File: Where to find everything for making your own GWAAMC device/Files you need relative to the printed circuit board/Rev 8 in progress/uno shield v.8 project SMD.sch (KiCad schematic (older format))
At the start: 108 parts, among them J1 Conn_3.5mm, J2 Power, J3 Analog, J4 Digital, J5 Digital, J6 Conn_01x09_Female, J6_A7,A6 Conn_01x02_gender_unknown, J7_A7,A6 Conn_01x02_Female, J9 TE_1-2328702-0, P1 CONN_01X01, P2 CONN_01X01, P3 CONN_01X01, P4 CONN_01X01, Q1 MMBF5460 (2N5460), Q2 MMBF5460 (2N5460), Q3 DMN601K-7, Q4 DMN601K-7, Q5 DMN601K-7, Q6 DMN601K-7, Q7 DMN601K-7, U1 3V LDO, U10 MCP4262-502E/UN, U11 MCP4262-502E/UN, U12 MCP4262-502E/UN, U13 MCP4262-502E/UN, U14 MCP4262-502E/UN, U15 MCP4262-502E/UN, U16 MCP4262-502E/UN, U17 MCP4262-502E/UN, U18 MCP4262-502E/UN, U19 MCP4262-502E/UN, U2 AD8244ARMZ, U20 MCP4262-502E/UN, U21 MCP4262-502E/UN, U22 MCP4262-502E/UN, U23 MCP4262-502E/UN, U24 MCP4262-502E/UN, U25 MCP4262-502E/UN, U26 MCP4262-502E/UN, U27 MCP4262-502E/UN, U28 MCP4262-502E/UN, U29 MCP4262-502E/UN, U3 ADL5315ACPZ-R7, U30 MCP4262-502E/UN, U31 MCP4262-502E/UN, U32 MCP4262-502E/UN, U33 MCP4262-502E/UN, U4 REF200AU, U5 LM334M, U6 LM334M, U7 MCP4262-503E/UN, U8 - U32 all in parallel MCP4262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, U9 MCP4262-502E/UN

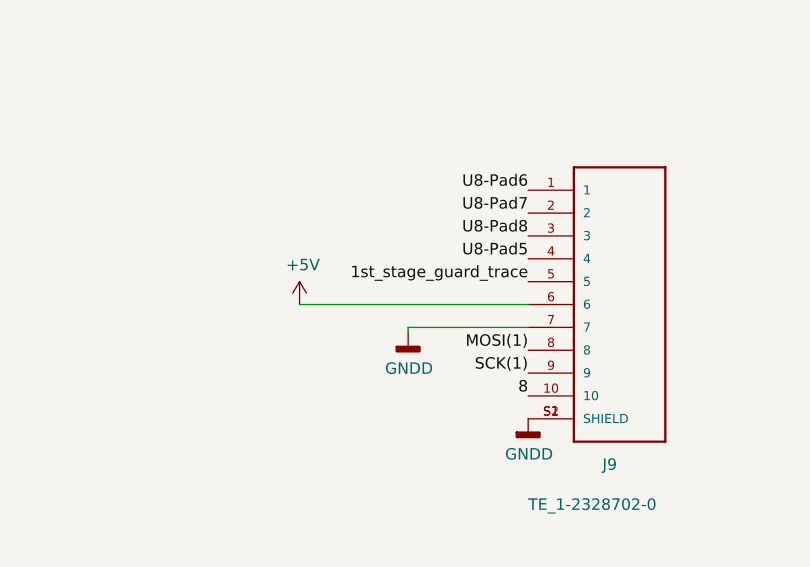
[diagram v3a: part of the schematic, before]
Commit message: Untested while awaiting bare PCB boards....
These KiCad and zipped gerber files are fully designed but not yet tested while I await the bare boards on order now.  I'm estimating mid- to late-October will see the final evaluation of operation of the entire device.  Shortly after that, I would expect to demonstrate its concepts and operation via YouTube and personal travel.
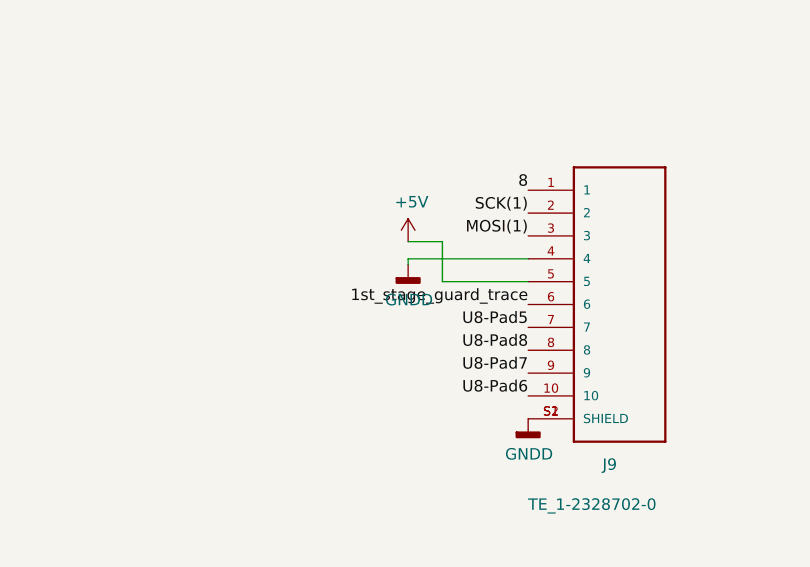
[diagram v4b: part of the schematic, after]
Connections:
- net +5V: now also J9.5; no longer J9.6
- net 1st_stage_guard_trace: now also J9.6; no longer J9.5
- net 8: now also J9.1; no longer J9.10
- net GNDD: now also J9.4; no longer J9.7
- net MOSI(1): now also J9.3; no longer J9.8
- net SCK(1): now also J9.2; no longer J9.9
- net U8-Pad5: now also J9.7; no longer J9.4
- net U8-Pad6: now also J9.10; no longer J9.1
- net U8-Pad7: now also J9.9; no longer J9.2
- net U8-Pad8: now also J9.8; no longer J9.3
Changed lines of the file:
@@
 L power:+5V #PWR0143
 U 1 1 5D764CDA
-P 3950 -800
-F 0 "#PWR0143" H 3950 -950 50  0001 C CNN
-F 1 "+5V" H 3965 -627 50  0000 C CNN
-F 2 "" H 3950 -800 50  0001 C CNN
-F 3 "" H 3950 -800 50  0001 C CNN
-	1    3950 -800
+P 4425 -1075
+F 0 "#PWR0143" H 4425 -1225 50  0001 C CNN
+F 1 "+5V" H 4440 -902 50  0000 C CNN
+F 2 "" H 4425 -1075 50  0001 C CNN
+F 3 "" H 4425 -1075 50  0001 C CNN
+	1    4425 -1075
 	1    0    0    -1
 $EndComp
-Text Label 4950 -400 2    50   ~ 0
+Text Label 4950 -1300 2    50   ~ 0
 8
-Text Label 4950 -500 2    50   ~ 0
+Text Label 4950 -1200 2    50   ~ 0
 SCK(1)
-Text Label 4950 -600 2    50   ~ 0
+Text Label 4950 -1100 2    50   ~ 0
 MOSI(1)
-Wire Wire Line
-	4950 -800 3950 -800
 $Comp
 L power:GNDD #PWR0144
 U 1 1 5D79F70A
-P 4425 -675
-F 0 "#PWR0144" H 4425 -925 50  0001 C CNN
-F 1 "GNDD" H 4429 -830 50  0000 C CNN
-F 2 "" H 4425 -675 50  0001 C CNN
-F 3 "" H 4425 -675 50  0001 C CNN
-	1    4425 -675
+P 4425 -975
+F 0 "#PWR0144" H 4425 -1225 50  0001 C CNN
+F 1 "GNDD" H 4429 -1130 50  0000 C CNN
+F 2 "" H 4425 -975 50  0001 C CNN
+F 3 "" H 4425 -975 50  0001 C CNN
+	1    4425 -975
 	1    0    0    -1
 $EndComp
-Text Label 4950 -1000 2    50   ~ 0
+Text Label 4950 -700 2    50   ~ 0
 U8-Pad5
-Text Label 4950 -1300 2    50   ~ 0
+Text Label 4950 -400 2    50   ~ 0
 U8-Pad6
-Text Label 4950 -1200 2    50   ~ 0
+Text Label 4950 -500 2    50   ~ 0
 U8-Pad7
-Text Label 4950 -1100 2    50   ~ 0
+Text Label 4950 -600 2    50   ~ 0
 U8-Pad8
 Wire Wire Line
-	4950 -700 4425 -700
+	4950 -1000 4425 -1000
 Wire Wire Line
-	4425 -700 4425 -675
-Text Label 4950 -900 2    50   ~ 0
+	4425 -1000 4425 -975
+Text Label 4950 -800 2    50   ~ 0
 1st_stage_guard_trace
 $Comp
@@
 Text Label 11450 4425 0    50   ~ 0
 8
+Wire Wire Line
+	4950 -900 4575 -900
+Wire Wire Line
+	4575 -900 4575 -1075
+Wire Wire Line
+	4575 -1075 4425 -1075
 $EndSCHEMATC

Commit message: Untested while awaiting bare PCB boards....
These KiCad and zipped gerber files are fully designed but not yet tested while I await the bare boards on order now.  I'm estimating mid- to late-October will see the final evaluation of operation of the entire device.  Shortly after that, I would expect to demonstrate its concepts and operation via YouTube and personal travel.
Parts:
- ADC1: Source Sockets: 1 qty SL-106-T-10 + 1 qty SMC-1-04-1-GT from http://Arrow.com. Component: least cost - https://www.aliexpress.com/item/1PCS-X-HX711-modules-weigh-sensors-for-AD-module-chip-preferred-DIY-Graduation/32851591970.html?spm=2114.search0104.3.1.7ad07d02cMfLjw&ws_ab_test=searchweb0_0,searchweb201602_4_10065_10130_10068_10890_10547_319_10546_317_10548_10545_10696_453_10084_454_10083_10618_10307_537_536_10059_10884_10887_321_322_10103,searchweb201603_52,ppcSwitch_0&algo_expid=c46a3ce9-e8cf-4d7c-8e89-50e4aff4f628-0&algo_pvid=c46a3ce9-e8cf-4d7c-8e89-50e4aff4f628&transAbTest=ae803_3; fastest arrival https://www.ebay.com/itm/Dual-Channel-HX711-Weighing-Pressure-Sensor-24-bit-Precision-A-D-Module-Arduino/202679288819?hash=item2f30a083f3:g:xyIAAOSwhXtc2wdH -> Sockets: 1 qty SL-106-T-10 + 1 qty SMC-1-04-1-GT from http://Arrow.com (sockets only, remember). Component: least cost - https://www.aliexpress.com/item/1PCS-X-HX711-modules-weigh-sensors-for-AD-module-chip-preferred-DIY-Graduation/32851591970.html?spm=2114.search0104.3.1.7ad07d02cMfLjw&ws_ab_test=searchweb0_0,searchweb201602_4_10065_10130_10068_10890_10547_319_10546_317_10548_10545_10696_453_10084_454_10083_10618_10307_537_536_10059_10884_10887_321_322_10103,searchweb201603_52,ppcSwitch_0&algo_expid=c46a3ce9-e8cf-4d7c-8e89-50e4aff4f628-0&algo_pvid=c46a3ce9-e8cf-4d7c-8e89-50e4aff4f628&transAbTest=ae803_3; fastest arrival https://www.ebay.com/itm/Dual-Channel-HX711-Weighing-Pressure-Sensor-24-bit-Precision-A-D-Module-Arduino/202679288819?hash=item2f30a083f3:g:xyIAAOSwhXtc2wdH
- C1: ClickToSortForPlacement 02 A duplicate C1 pad set is on PCB. Determine which pad se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 -> 02 A tiny 0201-size duplicate C1 pad set is on PCB. Determi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
- FID1, FID2, FID3, FID4, FID5, FID6: Source (none) -> 0 For clarity: [If not shown] U9-U33 must be ordered as wel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
- JP1: ClickToSortForPlacement 00 (TIPS - Always when sorting this page, make the column's title cell show the little sort direction indicator highlighted and pointing up. Solder temperature if using a soldering iron: Highest temperature solder when used for two-lead SMD components so they aren't so easily dislocated when bumped with hot iron. Never allow leaded solder to cross contaminate low-temp [bismuth] solders - lead ruins them. Plated through holes can only be used once on new boards unless they are HASL and you are careful to match solders with the factory solder or you are prepared to ream out plating-contaminated solder from the hole, so do NOT assume that tinning plated through holes to prepare the holes themselves for pins or leads is the right thing to do! Just use them as-is when the time comes even though they won't take the solder as well, or instead you may plug the holes with stainless steel paste dispensing syringe needle/nozzle 20-21 gauge while you tin the annular ring only on the one side oppo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 -> 00 (TIPS - Always when sorting this page, make the column's title cell show the little sort direction indicator highlighted and pointing up. Solder temperature if using a soldering iron: Highest temperature solder when used for two-lead SMD components so they aren't so easily dislocated when bumped with hot iron. Never allow leaded solder to cross contaminate low-temp [bismuth] solders - lead ruins them. Plated through holes can only be used once on new boards unless they are HASL and you are careful to match solders with the factory solder or you are prepared to ream out plating-contaminated solder from the hole, so do NOT assume that tinning plated through holes to prepare the holes themselves for pins or leads is the right thing to do! Just use them as-is when the time comes even though they won't take the solder as well, or instead you may plug the holes with stainless steel paste dispensing syringe needle/nozzle 20-21 gauge while you tin the annular ring only on the one side oppo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
- P1, P2, P3, P4: Source n/a -> 0 For clarity: [If not shown] U9-U33 must be ordered as wel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
- U10, U11, U12, U13, U14, U15, U16, U17, U18, U19, U20, U21, U22, U23, U24, U25, U26, U27, U28, U29, U30, U31, U32, U33, U9: Source http://www.digikey.com -> http://digikey.com
- U7: Source http://www.Arrow.com -> http://Arrow.com
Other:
- note added: "1 step MSB is 50000 ohms per device/256 steps per device = 195.3125 ohms = 195 ohms\n\n 5000 ohms LSB:\na single LSB device full resistance is 5000 ohms per device\n\nnumber of LSB devices to parallel together to make their full resistance value equal to 195 ohms is 5000 ohms per device/195 ohms = 25.6 devices\n\ncost = $25 + flex board a little larger size\n\n Alternate design under consideratio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"
- note added: "· 1 roll Polyimide (Kapton) tape 3/8" wide 6' length or greater. Use as electrical insulator and place assist. P/N 3057 from Arrow \nor equivalent\n· 38ga magnet wire for trace repairs. P/N 3522 from Arrow or equivalent\n· Solder wick P/N TOL-09327 from Arrow or equivalent\n· Soldering colophony (pine or gum ROSIN - NOT with zinc or ammonium chloride) flux (can make it yourself)\n· RG316 Coaxial 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"
- note removed: "1 roll Polyimide tape 3/8" wide 6' length or greater. Use as electrical insulator and place assist. P/N 3057 from Arrow or equivalent\n\n38ga magnet wire for U8+ and for trace repairs. P/N 3522 from Arrow or equivalent\nVery high temp solder (K100) not allowed on U3.\nThe best solder will always be "No Heat SAC305" if you can find it, but you still MUST cleanse gold from pads.\nAvoid Pb (leaded) 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"
- moved on the sheet: J9

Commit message: Untested while I'm building it out
These KiCad and zipped gerber files are fully designed but not yet tested while I'm building the bare boards now.  I'm estimating mid- to late-October will see the final evaluation of operation of the entire device.
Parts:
- ICSP1: ClickToSortForPlacement 19 Remove the previous JP6 wire and hold the full-size JP6 in its place while placing this. Set height with all connectors to MCU mated, some connectors may need spaced away from board or otherwise made to fit. Then check work for inadvertent shorts and opens. Replace JP6, if removed, with the style you want - wire or removeable shunt. Apply Kapton tape anywhere needed as board is mated to MCU, while also ensuring no Vcc conflicts will exist. -> 19 Remove the previous JP6 wire and hold the full-size JP6 in its place while placing this. Set height with all connectors to MCU mated, some connectors may need spaced away from board or otherwise made to fit. Place using bismuth solder if you have it (provided you used no-lead solder to pre-tin with) for easiest removal. Then check work for inadvertent shorts and opens. Replace JP6, if removed, with the style you want - wire or removeable shunt. Apply Kapton tape anywhere needed as board is mated to MCU, while also ensuring no Vcc conflicts will exist.
- J2: ClickToSortForPlacement 20 When MCU is NOT 5V, pin 5 gets removed and pin 4 gets its pad shorted to pin 5 PAD. When MCU is switchable 5V and 3.3V and you want to be able to switch between the two levels, remove pin 5 still but tie ICSP1 pin 2 into pin 5 PAD with an insulated wire. Height with all connectors mated, may need to space away from board some. Then check work for inadvertent shorts and opens. -> 20 When MCU is NOT 5V, pin 5 gets removed and pin 4 gets its pad shorted to pin 5 PAD. When MCU is switchable 5V and 3.3V and you want to be able to switch between the two levels, remove pin 5 still but tie ICSP1 pin 2 into pin 5 PAD with an insulated wire. Height with all connectors mated, may need to space away from board some. Place with dessicant inside using bismuth solder if you have it for easiest removal (provided you used no-lead solder to pre-tin with) . Then check work for inadvertent shorts and opens.
- J3, J4: ClickToSortForPlacement 20 Placing into plated-through holes requires more solder t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 -> 20 Requires more solder than single-sided components and he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
- J5: ClickToSortForPlacement 21 Set height with all connectors mated, may need to space away from board some. Placing into plated-through holes requires more solder than single-sided components and heat for a longer time or the MCU can push the solder pads right off the board. Then check work for inadvertent shorts and opens. Power up and run diags. Power down and continue. -> 21 Set height with all connectors mated, may need to space away from board some. Requires more solder than single-sided components and heat for a longer time or the MCU can push the solder pads right off the board. Use bismuth solder if you have it for easiest removal (provided you used no-lead solder to pre-tin with). Then check work for inadvertent shorts and opens. Power up and run diags. Power down and continue.
- JP1: footprint Jumper:SolderJumper-3_P1.3mm_Open_RoundedPad1.0x1.5mm_NumberLabels -> Jumper:SolderJumper-3_P1.3mm_Bridged12_RoundedPad1.0x1.5mm_NumberLabels; symbol Jumper:SolderJumper_3_Open -> Jumper:SolderJumper_3_Bridged12; ClickToSortForPlacement 00 (TIPS - Always when sorting this page, make the column's title cell show the little sort direction indicator highlighted and pointing up. Solder temperature if using a soldering iron: Highest temperature solder when used for two-lead SMD components so they aren't so easily dislocated when bumped with hot iron. Never allow leaded solder to cross contaminate low-temp [bismuth] solders - lead ruins them. Plated through holes can only be used once on new boards unless they are HASL and you are careful to match solders with the factory solder or you are prepared to ream out plating-contaminated solder from the hole, so do NOT assume that tinning plated through holes to prepare the holes themselves for pins or leads is the right thing to do! Just use them as-is when the time comes even though they won't take the solder as well, or instead you may plug the holes with stainless steel paste dispensing syringe needle/nozzle 20-21 gauge while you tin the annular ring only on the one side oppo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 -> 00 (TIPS - Always when sorting this page, make the column's title cell show the little sort direction indicator highlighted and pointing up. Solder temperature if using a soldering iron: Use your highest temperature solder for two-lead SMD components so they aren't so easily dislocated later when accidentally bumped with hot iron. Never allow leaded solder to cross contaminate low-temp [bismuth] solders - lead ruins them. Do your best to keep SMD component leads clean from adhesive tape glue and other sticky, clingy, slimy contaminates that could leave a film where solder will need to adhere to them. Plated through holes can only be used once on new boards unless they are Hot Air Solder Leveled [HASL] and you are careful to match solders with the factory solder or you are prepared to ream out plating-contaminated solder from the hole, so do NOT assume that tinning plated through holes to prepare the holes themselves for pins or leads is the right thing to do! Just use them as-is when 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
- JP2: footprint Jumper:SolderJumper-3_P1.3mm_Open_RoundedPad1.0x1.5mm_NumberLabels -> Jumper:SolderJumper-3_P1.3mm_Bridged12_RoundedPad1.0x1.5mm_NumberLabels; symbol Jumper:SolderJumper_3_Open -> Jumper:SolderJumper_3_Bridged12
- R17: ClickToSortForPlacement 14 IF NO FOOTPRINT FOR THIS: OPTIONAL IN BOARD REV 7 AND BE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 -> 14 IF NO FOOTPRINT FOR THIS: OPTIONAL IN BOARD REV .7 AND B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
- R5: ClickToSortForPlacement 05 Place, then check work as before. The steps up to this one were to install amplification stability ckt for powering up U2. Pwr supply stability ckts for U1 and ADC1 are next after diagnostics of the work you've done so far: You have reached the step of applying power voltage to the board, and you MUST not make any mistakes doing so or you'll all too likely damage components that will cost you extra shipping, handling to replace. As you prepare to continue, be fully aware that any mistakes you make can destroy components when power gets applied. BE VERY OBSERVANT. Determine which of +5V or +3V3 your MCU puts on ICSP1 pin 2 before applying MCU power to this board: 5V is default of this PCB design. If the MCU instead puts 3V on the ICSP1 pin 2, you MUST modify this board at J2 pins 4 & 5 or you'll stress out your MCU and likely damage it! Such modification inflexibly renders this board unfit for 5V operation since there was not room for jumpers to make this change flexible. You will b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 -> 05 Place, then check work as before. The steps up to this one were to install first stage stability ckt for powering up U3. Pwr supply stability ckts for U1 and ADC1 are next after diagnostics of the work you've done so far: You have reached the step of applying power voltage to the board, and you MUST not make any mistakes doing so or you'll all too likely damage components that will cost you extra shipping, handling to replace. As you prepare to continue, be fully aware that any mistakes you make can destroy components when power gets applied. BE VERY OBSERVANT. Determine which of +5V or +3V3 your MCU puts on ICSP1 pin 2 before applying MCU power to this board: 5V is default of this PCB design. If the MCU instead puts 3V on the ICSP1 pin 2, you MUST modify this board at J2 pins 4 & 5 or you'll stress out your MCU and likely damage it! Such modification inflexibly renders this board unfit for 5V operation since there was not room for jumpers to make this change flexible. You will bri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
- SHLD1: ClickToSortForPlacement 27 Thoroughly solder in place with dessicant inside. Verify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 -> 27 Verify every place-assist hole inside shield footprint i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
- U10: renamed from U13; ClickToSortForPlacement 15 NOT WELL ACCOMMODATED ON BOARD REV 7 AND BELOW: PATCHING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 -> 15 NOT WELL ACCOMMODATED ON BOARD REV .7 AND BELOW: PATCHIN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
- U11: renamed from U17; ClickToSortForPlacement 15 NOT WELL ACCOMMODATED ON BOARD REV 7 AND BELOW: PATCHING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 -> 15 NOT WELL ACCOMMODATED ON BOARD REV .7 AND BELOW: PATCHIN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
- U12: renamed from U21; ClickToSortForPlacement 15 NOT WELL ACCOMMODATED ON BOARD REV 7 AND BELOW: PATCHING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 -> 15 NOT WELL ACCOMMODATED ON BOARD REV .7 AND BELOW: PATCHIN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
- U13: renamed from U25; ClickToSortForPlacement 15 NOT WELL ACCOMMODATED ON BOARD REV 7 AND BELOW: PATCHING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 -> 15 NOT WELL ACCOMMODATED ON BOARD REV .7 AND BELOW: PATCHIN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
- U14: renamed from U29; ClickToSortForPlacement 15 NOT WELL ACCOMMODATED ON BOARD REV 7 AND BELOW: PATCHING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 -> 15 NOT WELL ACCOMMODATED ON BOARD REV .7 AND BELOW: PATCHIN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
- U15: renamed from U10; ClickToSortForPlacement 15 NOT WELL ACCOMMODATED ON BOARD REV 7 AND BELOW: PATCHING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 -> 15 NOT WELL ACCOMMODATED ON BOARD REV .7 AND BELOW: PATCHIN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
- U16: renamed from U14; ClickToSortForPlacement 15 NOT WELL ACCOMMODATED ON BOARD REV 7 AND BELOW: PATCHING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 -> 15 NOT WELL ACCOMMODATED ON BOARD REV .7 AND BELOW: PATCHIN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
- U17: renamed from U18; ClickToSortForPlacement 15 NOT WELL ACCOMMODATED ON BOARD REV 7 AND BELOW: PATCHING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 -> 15 NOT WELL ACCOMMODATED ON BOARD REV .7 AND BELOW: PATCHIN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
- U18: renamed from U22; ClickToSortForPlacement 15 NOT WELL ACCOMMODATED ON BOARD REV 7 AND BELOW: PATCHING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 -> 15 NOT WELL ACCOMMODATED ON BOARD REV .7 AND BELOW: PATCHIN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
- U19: renamed from U26; ClickToSortForPlacement 15 NOT WELL ACCOMMODATED ON BOARD REV 7 AND BELOW: PATCHING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 -> 15 NOT WELL ACCOMMODATED ON BOARD REV .7 AND BELOW: PATCHIN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
- U20: renamed from U30; ClickToSortForPlacement 15 NOT WELL ACCOMMODATED ON BOARD REV 7 AND BELOW: PATCHING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 -> 15 NOT WELL ACCOMMODATED ON BOARD REV .7 AND BELOW: PATCHIN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
- U21: renamed from U11; ClickToSortForPlacement 15 NOT WELL ACCOMMODATED ON BOARD REV 7 AND BELOW: PATCHING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 -> 15 NOT WELL ACCOMMODATED ON BOARD REV .7 AND BELOW: PATCHIN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
- U22: renamed from U15; ClickToSortForPlacement 15 NOT WELL ACCOMMODATED ON BOARD REV 7 AND BELOW: PATCHING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 -> 15 NOT WELL ACCOMMODATED ON BOARD REV .7 AND BELOW: PATCHIN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
- U23: renamed from U19; ClickToSortForPlacement 15 NOT WELL ACCOMMODATED ON BOARD REV 7 AND BELOW: PATCHING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 -> 15 NOT WELL ACCOMMODATED ON BOARD REV .7 AND BELOW: PATCHIN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
- U24: renamed from U23; ClickToSortForPlacement 15 NOT WELL ACCOMMODATED ON BOARD REV 7 AND BELOW: PATCHING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 -> 15 NOT WELL ACCOMMODATED ON BOARD REV .7 AND BELOW: PATCHIN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
- U25: renamed from U27; ClickToSortForPlacement 15 NOT WELL ACCOMMODATED ON BOARD REV 7 AND BELOW: PATCHING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 -> 15 NOT WELL ACCOMMODATED ON BOARD REV .7 AND BELOW: PATCHIN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
- U26: renamed from U31; ClickToSortForPlacement 15 NOT WELL ACCOMMODATED ON BOARD REV 7 AND BELOW: PATCHING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 -> 15 NOT WELL ACCOMMODATED ON BOARD REV .7 AND BELOW: PATCHIN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
- U27: renamed from U12; ClickToSortForPlacement 15 NOT WELL ACCOMMODATED ON BOARD REV 7 AND BELOW: PATCHING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 -> 15 NOT WELL ACCOMMODATED ON BOARD REV .7 AND BELOW: PATCHIN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
- U28: renamed from U16; ClickToSortForPlacement 15 NOT WELL ACCOMMODATED ON BOARD REV 7 AND BELOW: PATCHING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 -> 15 NOT WELL ACCOMMODATED ON BOARD REV .7 AND BELOW: PATCHIN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
- U29: renamed from U20; ClickToSortForPlacement 15 NOT WELL ACCOMMODATED ON BOARD REV 7 AND BELOW: PATCHING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 -> 15 NOT WELL ACCOMMODATED ON BOARD REV .7 AND BELOW: PATCHIN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
- U30: renamed from U24; ClickToSortForPlacement 15 NOT WELL ACCOMMODATED ON BOARD REV 7 AND BELOW: PATCHING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 -> 15 NOT WELL ACCOMMODATED ON BOARD REV .7 AND BELOW: PATCHIN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
- U31: renamed from U28; ClickToSortForPlacement 15 NOT WELL ACCOMMODATED ON BOARD REV 7 AND BELOW: PATCHING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 -> 15 NOT WELL ACCOMMODATED ON BOARD REV .7 AND BELOW: PATCHIN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
- U32, U33, U9: ClickToSortForPlacement 15 NOT WELL ACCOMMODATED ON BOARD REV 7 AND BELOW: PATCHING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 -> 15 NOT WELL ACCOMMODATED ON BOARD REV .7 AND BELOW: PATCHIN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
- U5, U6: ClickToSortForPlacement 23 Check corner pads for adequate bare metal: ensure the solder mask of all corner pads is scraped off. Before placing, run the diags that use the ohmmeter. Place then check work. Place short between pins 2 and 5 of U3 and place 1.5 MOhm from Q2 pins 1 & 2 to GND. Place a short between pins 1 & 2 of Q1. Make sure the added shorts cannot get bumped so to lift the pads they attach to. Run diags. Remove shorts on Q1 and Q2. -> 23 Check corner pads for adequate bare metal: ensure the solder mask of all corner pads is scraped off. Before placing, run the diags that use the ohmmeter. Place then check work, you may allow up to three of pins 5-8 to fly free since none of them have electrical connection. Place short between pins 2 and 5 of U4 and place 1.5 MOhm from Q2 pins 1 & 2 to GND. Place a short between pins 1 & 2 of Q1. Make sure the added shorts cannot get bumped so to lift the pads they attach to. Run diags. Remove shorts on Q1 and Q2.
- U8: value - U32 all in parallel MCP4262-502E/UN -> - U33 all in parallel MCP4262-502E/UN
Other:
- note added: "· 1 roll Polyimide (Kapton) tape 3/8" wide 6' length or greater. Use as electrical insulator and place assist. P/N 3057 from Arrow \nor equivalent\n· 38ga magnet wire for trace repairs. P/N 3522 from Arrow or equivalent\n· Solder wick P/N TOL-09327 from Arrow or equivalent\n· Soldering colophony (pine or gum ROSIN - NOT with zinc nor ammonium chlorides) flux (can make it yourself)\n· RG316 Coaxia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"
- note removed: "· 1 roll Polyimide (Kapton) tape 3/8" wide 6' length or greater. Use as electrical insulator and place assist. P/N 3057 from Arrow \nor equivalent\n· 38ga magnet wire for trace repairs. P/N 3522 from Arrow or equivalent\n· Solder wick P/N TOL-09327 from Arrow or equivalent\n· Soldering colophony (pine or gum ROSIN - NOT with zinc or ammonium chloride) flux (can make it yourself)\n· RG316 Coaxial 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"
